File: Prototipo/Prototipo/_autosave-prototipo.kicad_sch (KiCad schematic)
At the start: 13 parts, among them J1 Conn_01x02_Socket, J4 Conn_01x12_Pin

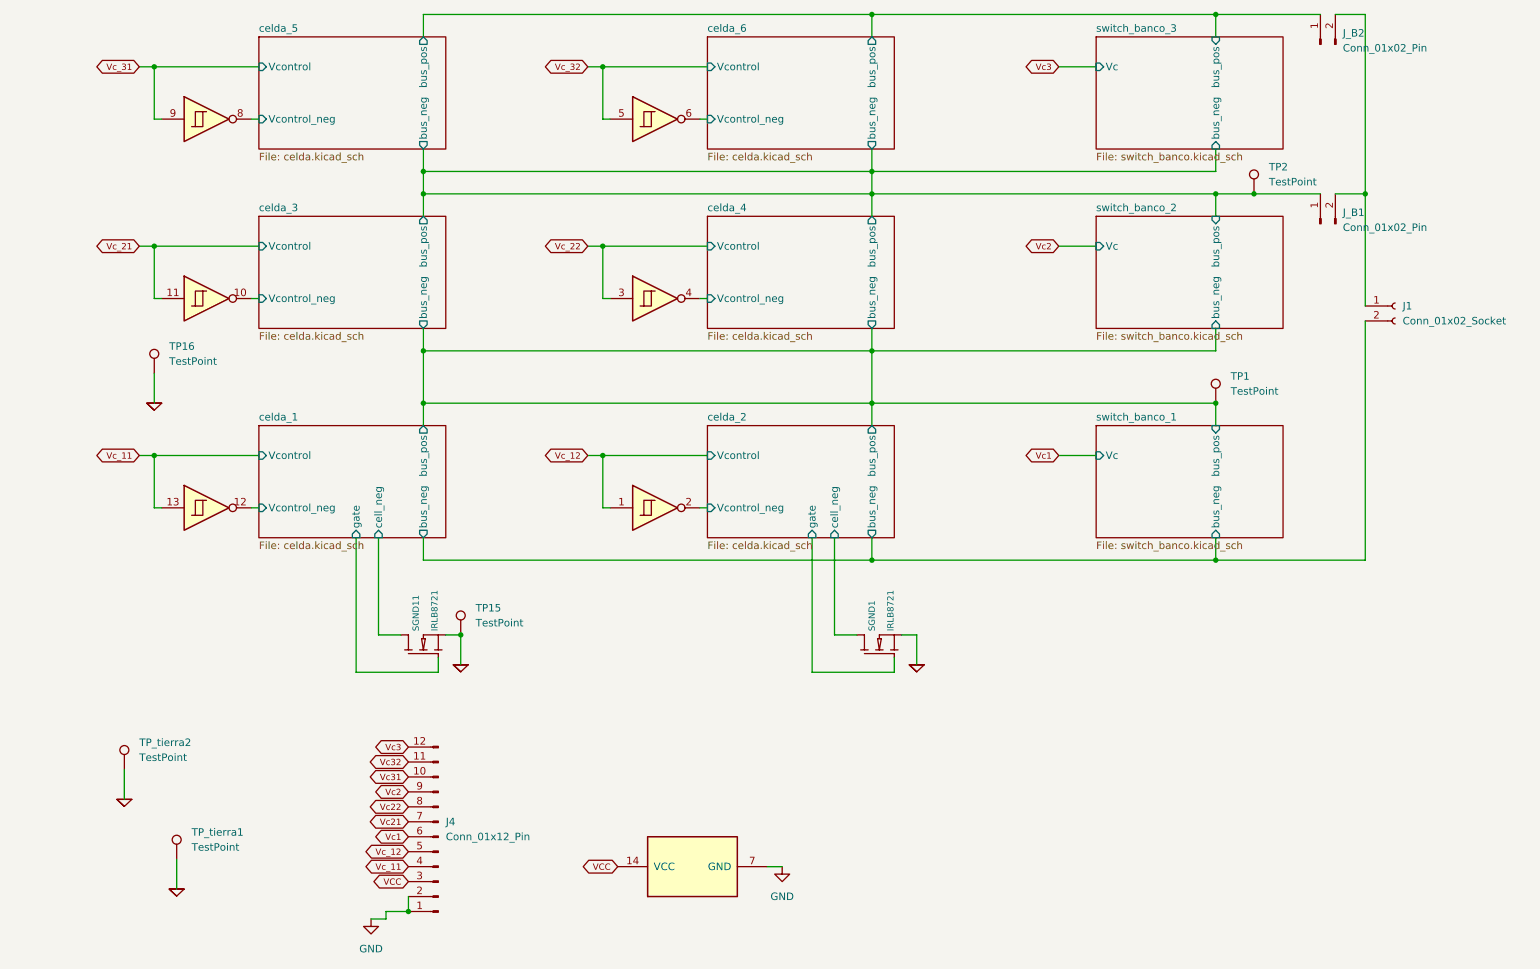
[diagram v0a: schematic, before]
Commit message: propuesta de disposición de los elementos del pcb
subo antes de empezar a hacer el ruteo
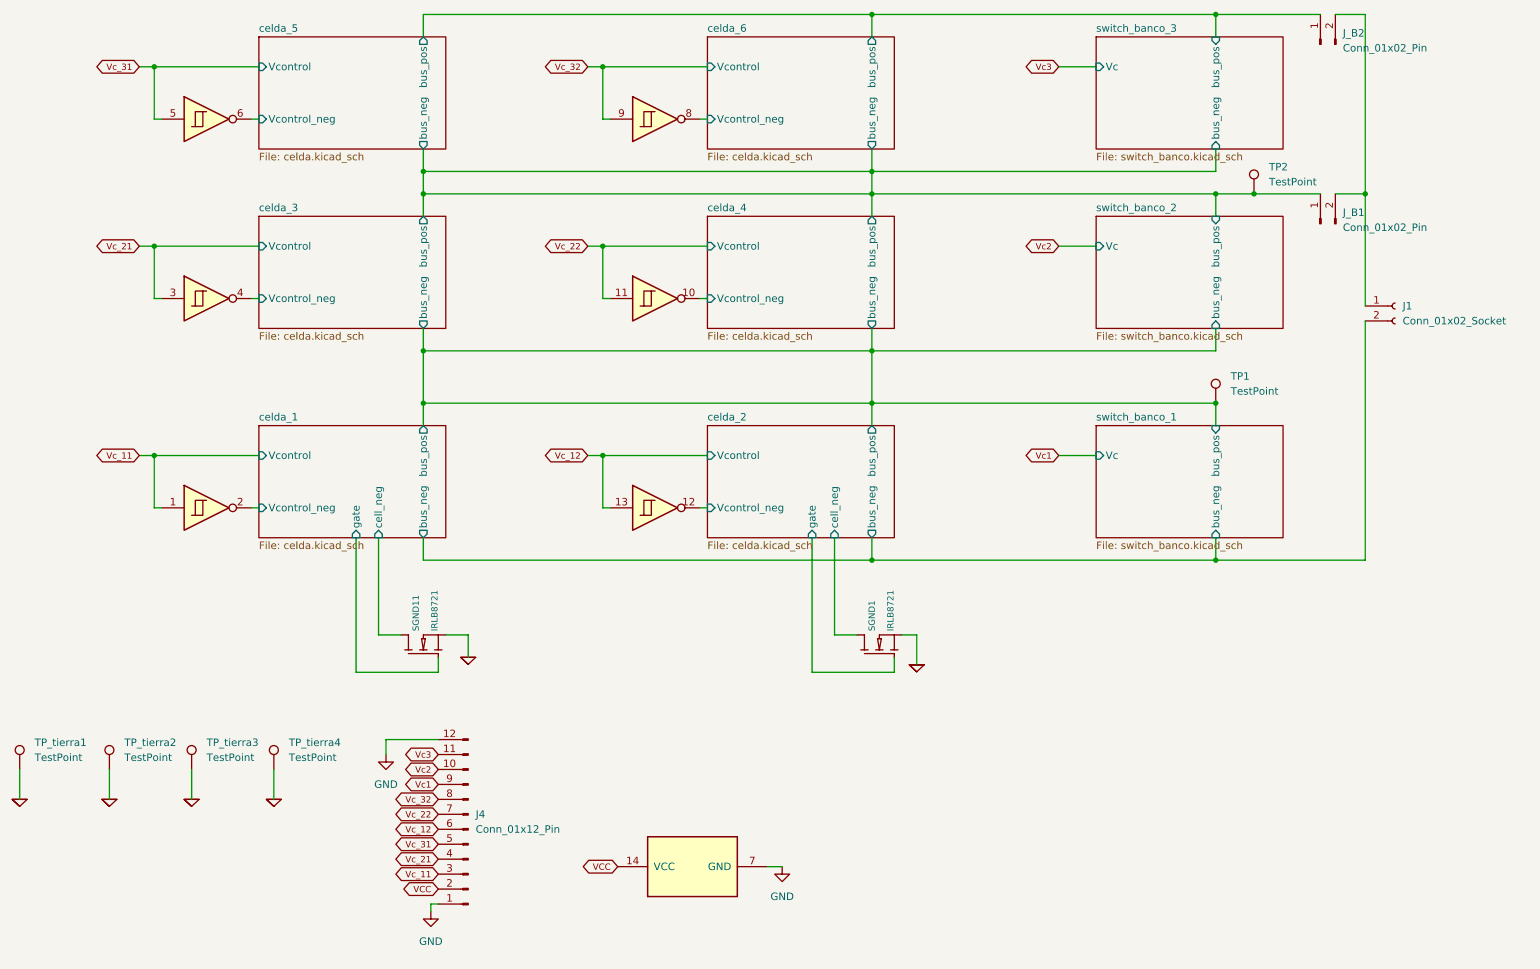
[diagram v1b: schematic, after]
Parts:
- J_B1, J_B2: footprint Connector_JST:JST_VH_B2P-VH_1x02_P3.96mm_Vertical -> Connector_PinHeader_2.54mm:PinHeader_1x02_P2.54mm_Vertical
- renumbered TP16 to TP_tierra3, TP15 to TP_tierra4
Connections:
- net Vc21 is gone; now on net Vc_22: J4.7 (Pin_7)
- net Vc22 is gone; now on net Vc_32: J4.8 (Pin_8)
- net Vc31 is gone; now on net Vc2: J4.10 (Pin_10)
- net Vc32 is gone; now on net Vc3: J4.11 (Pin_11)
- net GND: now also J4.12 (Pin_12); no longer J4.2 (Pin_2)
- net VCC: now also J4.2 (Pin_2); no longer J4.3 (Pin_3)
- net Vc1: now also J4.9 (Pin_9); no longer J4.6 (Pin_6)
- net Vc2: no longer J4.9 (Pin_9)
- net Vc3: no longer J4.12 (Pin_12)
- net Vc_11: now also A1.1, J4.3 (Pin_3); no longer A1.13, J4.4 (Pin_4)
- net Vc_12: now also A1.13, J4.6 (Pin_6); no longer A1.1, J4.5 (Pin_5)
- net Vc_21: now also A1.3, J4.4 (Pin_4); no longer A1.11
- net Vc_22: now also A1.11; no longer A1.3
- net Vc_31: now also A1.5, J4.5 (Pin_5); no longer A1.9
- net Vc_32: now also A1.9; no longer A1.5
- net celda_1/Vcontrol_neg: now also A1.2; no longer A1.12
- net celda_2/Vcontrol_neg: now also A1.12; no longer A1.2
- net celda_3/Vcontrol_neg: now also A1.4; no longer A1.10
- net celda_4/Vcontrol_neg: now also A1.10; no longer A1.4
- net celda_5/Vcontrol_neg: now also A1.6; no longer A1.8
- net celda_6/Vcontrol_neg: now also A1.8; no longer A1.6
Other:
- moved on the sheet: J4, TP_tierra1, TP_tierra2, TP_tierra3, TP_tierra4
